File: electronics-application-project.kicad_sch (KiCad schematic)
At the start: 52 parts, among them J1 Conn_02x03_Odd_Even, J2 Conn_01x02_Pin, J3 Conn_01x02_Pin, J4 Conn_01x02_Pin, U1 W5500, U2 ARJM11C7-114-BA-EW2, U3 LM2574-3.3YN, U4 ATTINY85-20SU, U5 74HC00, Y2 ABLS7M2-25.000MHZ-D-2Y-T

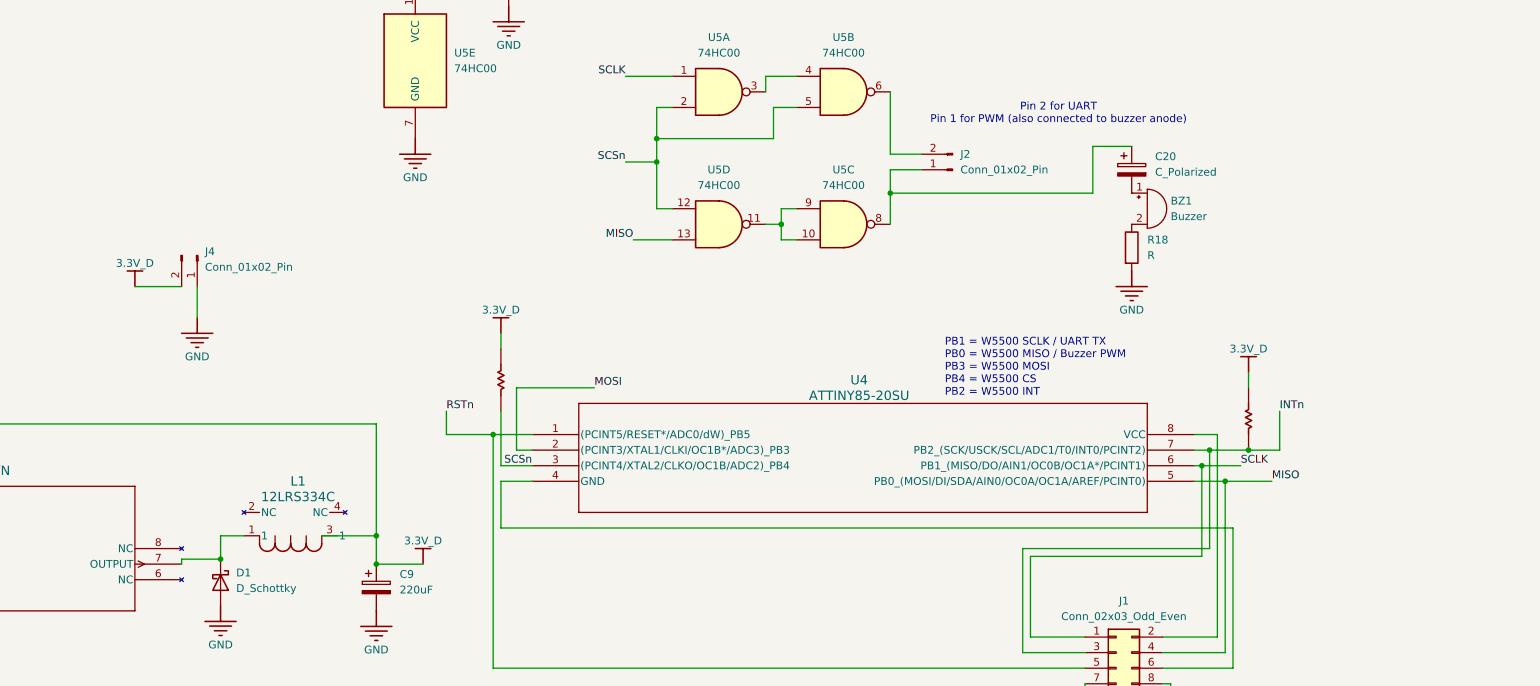
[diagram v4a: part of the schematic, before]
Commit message: connect attiny85 to GND and 3.3V_D rails; remove redundant pin header;
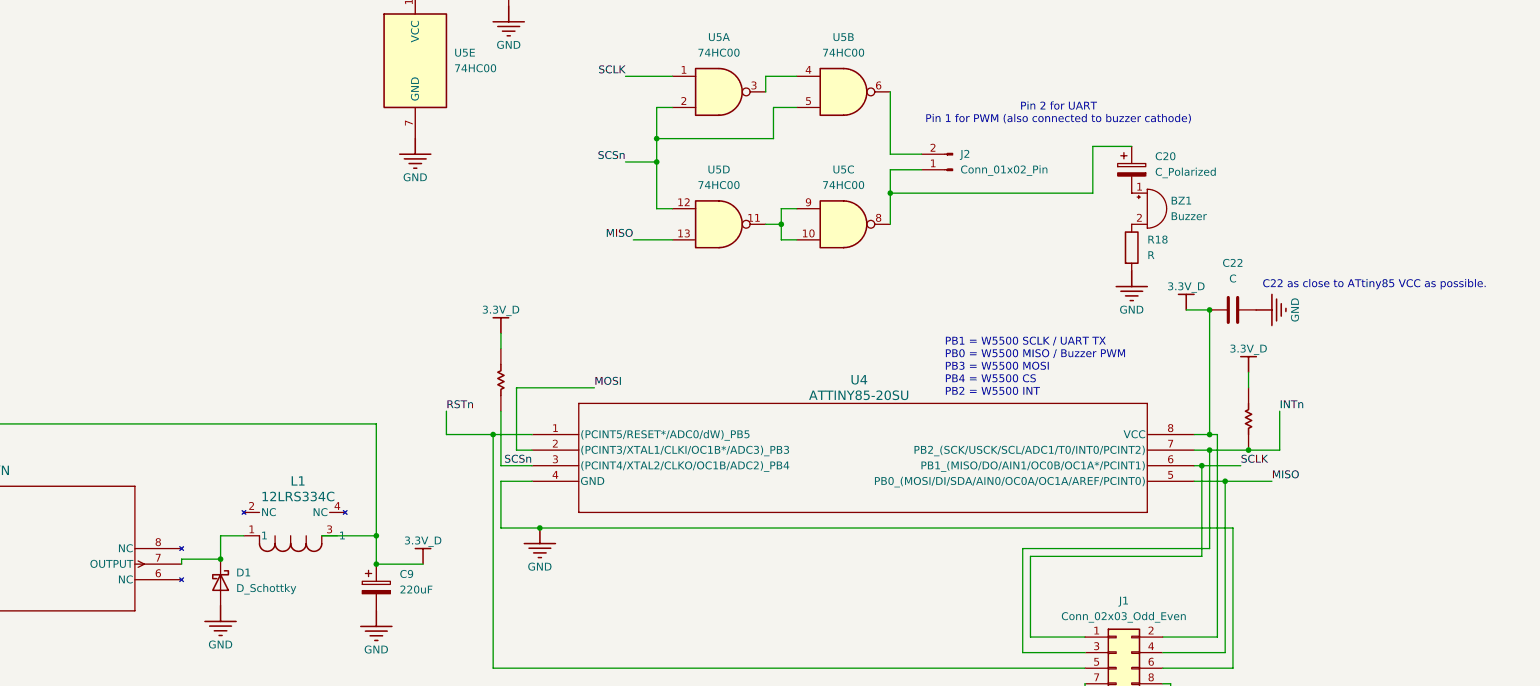
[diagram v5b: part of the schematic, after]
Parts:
- removed J4: Conn_01x02_Pin, Connector_PinHeader_2.54mm:PinHeader_1x02_P2.54mm_Vertical, symbol Connector:Conn_01x02_Pin
- added C22: C, symbol Device:C
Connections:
- net 3.3V_D: now also J1.2 (Pin_2), U4.8 (VCC), C22.2
- net GND: now also J1.6 (Pin_6), U4.4 (GND), C22.1
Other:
- note added: "C22 as close to ATtiny85 VCC as possible."
- note added: "Pin 2 for UART Pin 1 for PWM (also connected to buzzer cathode)"
- note removed: "Pin 2 for UART Pin 1 for PWM (also connected to buzzer anode)"

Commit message: update pcb from schematic
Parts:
- C22: footprint (none) -> Capacitor_SMD:C_0805_2012Metric_Pad1.18x1.45mm_HandSolder
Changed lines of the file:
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@@
 			)
 		)
-		(property "Footprint" ""
+		(property "Footprint" "Capacitor_SMD:C_0805_2012Metric_Pad1.18x1.45mm_HandSolder"
 			(at 337.82 92.4052 0)
 			(effects

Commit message: DRC pass
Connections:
- net MISO: now also J1.8 (Pin_8), U4.2 ((PCINT3/XTAL1/CLKI/OC1B*/ADC3)_PB3); no longer J1.4 (Pin_4), U4.5 (PB0_(MOSI/DI/SDA/AIN0/OC0A/OC1A/AREF/PCINT0)), U5.13
- net MOSI: now also J1.4 (Pin_4), U4.5 (PB0_(MOSI/DI/SDA/AIN0/OC0A/OC1A/AREF/PCINT0)), U5.13; no longer J1.8 (Pin_8), U4.2 ((PCINT3/XTAL1/CLKI/OC1B*/ADC3)_PB3)
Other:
- note added: "PB1 = W5500 SCLK / UART TX PB0 = W5500 MOSI / Buzzer PWM PB3 = W5500 MISO PB4 = W5500 CS PB2 = W5500 INT"
- note removed: "PB1 = W5500 SCLK / UART TX PB0 = W5500 MISO / Buzzer PWM PB3 = W5500 MOSI PB4 = W5500 CS PB2 = W5500 INT"
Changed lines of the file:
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@@
 		)
 	)
-	(text "PB1 = W5500 SCLK / UART TX\nPB0 = W5500 MISO / Buzzer PWM\nPB3 = W5500 MOSI\nPB4 = W5500 CS\nPB2 = W5500 INT"
+	(text "PB1 = W5500 SCLK / UART TX\nPB0 = W5500 MOSI / Buzzer PWM\nPB3 = W5500 MISO\nPB4 = W5500 CS\nPB2 = W5500 INT"
 		(exclude_from_sim no)
 		(at 294.64 100.838 0)
@@
 		)
 	)
-	(label "MISO"
+	(label "MOSI"
 		(at 243.84 80.01 180)
 		(effects
@@
 		)
 	)
-	(label "MOSI"
+	(label "MISO"
 		(at 237.49 104.14 0)
 		(effects
@@
 		)
 	)
-	(label "MOSI"
+	(label "MISO"
 		(at 331.47 154.94 270)
 		(effects
@@
 		)
 	)
-	(label "MISO"
+	(label "MOSI"
 		(at 347.98 119.38 0)
 		(effects
